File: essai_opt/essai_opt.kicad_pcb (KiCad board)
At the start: 2 copper layers, 41.5 x 44.5 mm, 26 parts, among them J1 Conn_01x20, J2 Conn_Coaxial, J3 Conn_01x02, J4 USB_C_Receptacle, U2 ESP32-C6-MINI-1/U

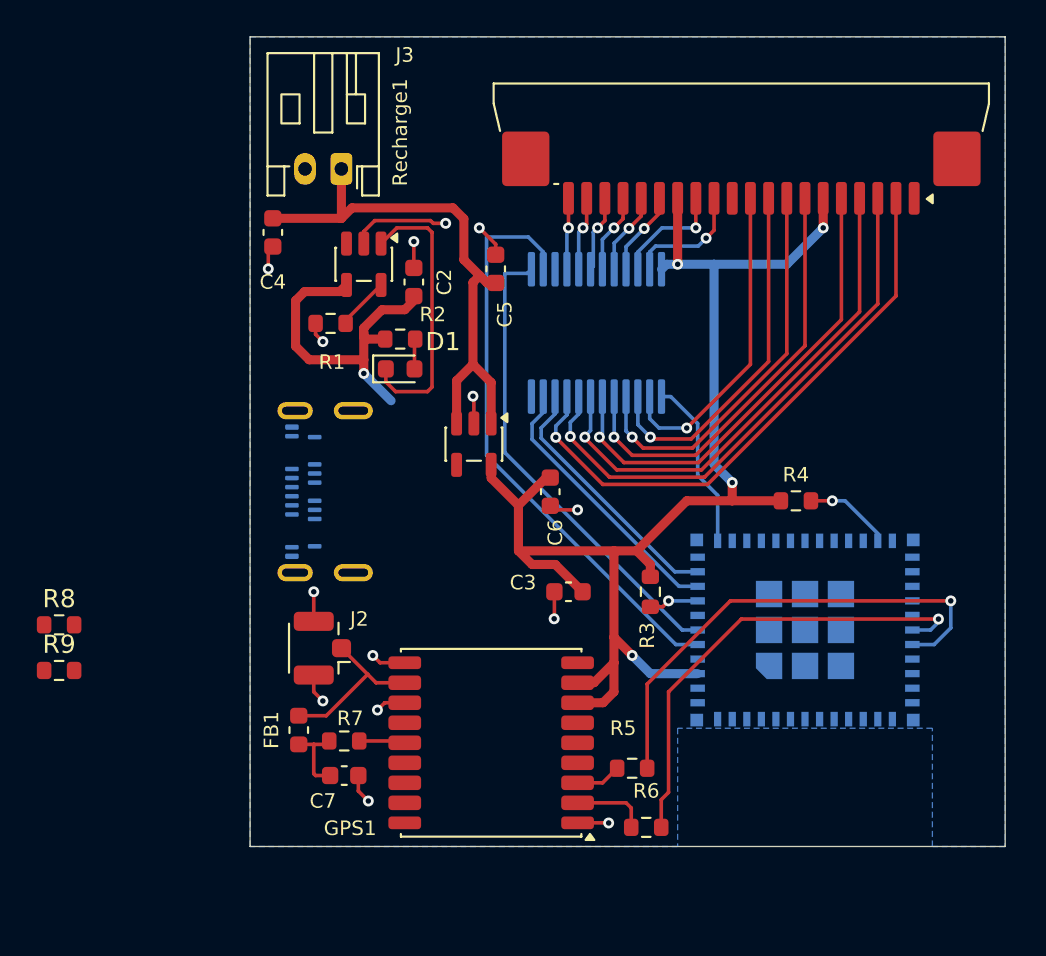
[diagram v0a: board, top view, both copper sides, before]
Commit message: Deuxième version usb-c
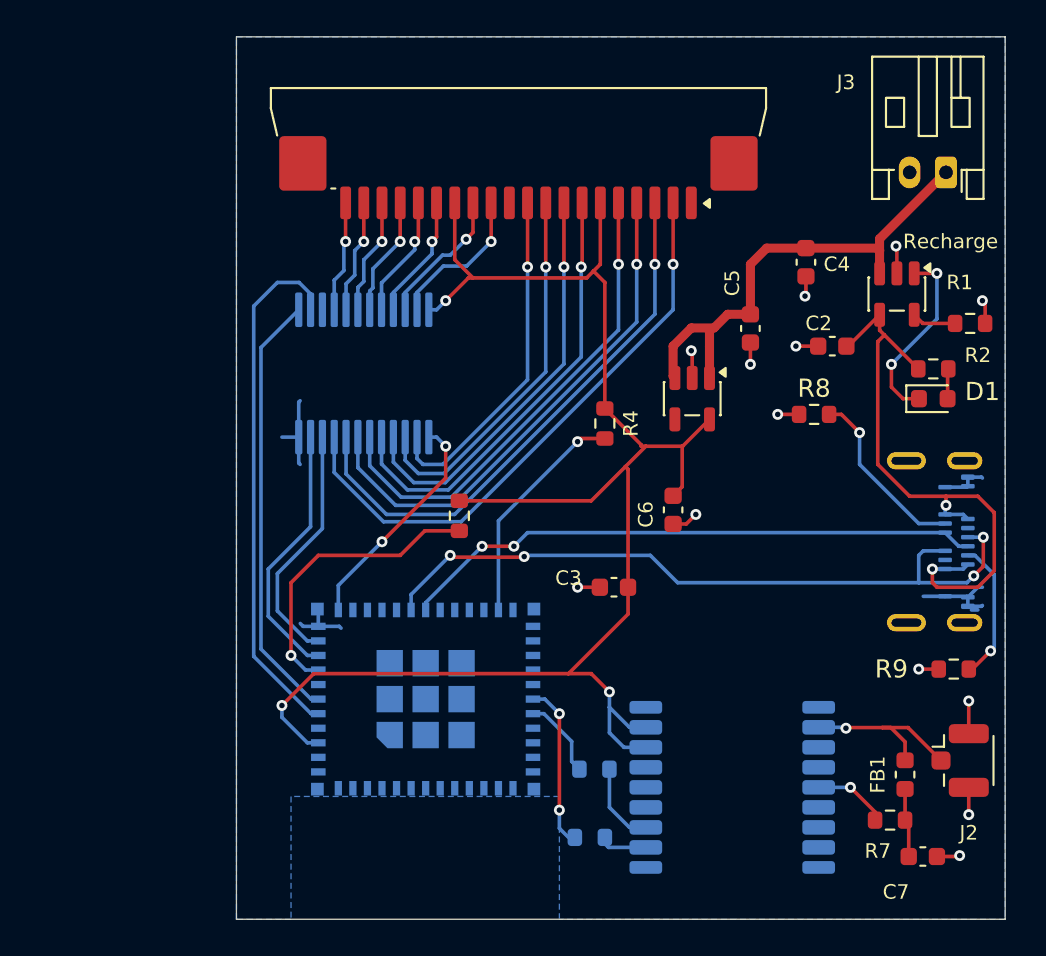
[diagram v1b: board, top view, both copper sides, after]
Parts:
- GPS1, R5, R6: moved to B.Cu
- moved R9 49.2 mm to (133.7, 135.2)
- moved R8 43.1 mm to (126.0, 121.2)
- moved J2 36.5 mm to (134.5, 140.3), turned to 0 degrees
- moved R1 35.1 mm to (134.6, 116.2), turned to 180 degrees
- moved FB1 33.4 mm to (131.0, 141.1)
- moved J3 33.2 mm to (133.2, 108.0)
- moved C7 32.1 mm to (132.0, 145.6)
- moved J4 30.9 mm to (131.2, 128.2), turned to 90 degrees
- moved R7 30.3 mm to (130.2, 143.6), turned to 180 degrees
- moved D1 29.3 mm to (132.6, 120.4)
- moved R2 29.3 mm to (132.6, 118.8)
- moved Recharge 29.3 mm to (130.6, 114.6)
- moved C4 29.3 mm to (125.5, 112.9)
- moved C2 23.3 mm to (127.0, 117.5), turned to 0 degrees
- moved U2 21.2 mm to (104.7, 139.6)
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- renumbered Recharge1 to Recharge
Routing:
- net Net-(U2-GPIO12/USB_D-): track 0.00 -> 39.8 mm, vias 0 -> 4
- net Net-(U2-GPIO13/USB_D+): track 0.00 -> 32.1 mm, vias 0 -> 2
- net RX GPS: track 27.2 -> 4.46 mm, vias 1 -> 0
- net TX GPS: track 25.9 -> 8.79 mm, vias 1 -> 2
- net VBUS: track 19.2 -> 33.4 mm, vias 1 -> 2
- net /ALIM 3V3: track 75.9 -> 90.1 mm, vias 4 -> 3
- net Net-(U2-EN/CHIP_PU): track 2.73 -> 16.3 mm
- net Net-(J4-CC2): track 0.00 -> 9.89 mm, vias 0 -> 1
- net Net-(U2-GPIO9): track 4.82 -> 12.6 mm
- net Net-(J4-CC1): track 0.00 -> 7.78 mm, vias 0 -> 1
- net GND: track 26.1 -> 33.0 mm, vias 14 -> 13
- net Net-(D1-K): track 15.7 -> 10.3 mm, vias 0 -> 2
- net Net-(J3-Pin_1): track 30.6 -> 26.6 mm
- net Net-(MUX1-S2): track 32.3 -> 28.9 mm
- net Net-(MUX1-COM): track 9.50 -> 12.6 mm, vias 0 -> 2
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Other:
- board size 41.5 x 44.5 mm -> 42.2 x 48.5 mm
